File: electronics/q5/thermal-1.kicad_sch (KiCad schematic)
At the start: 6 parts, among them Q3 Charge enable, Q4 Charge enable hot gate

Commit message: Q5 design lock: JLC Basic substitutions, re-verified board, cost estimator
Co-Authored-By: Claude Opus 5.5 <noreply@anthropic.com>
Claude-Session: https://claude.ai/code/session_01UrkzLMrBi6iLPSL5SbMCA7
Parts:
- C9: MPN GRM188R71H104KA93D -> CC0603KRX7R9BB104
- Q3, Q4: MPN 2N7002,215 -> 2N7002
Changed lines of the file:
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@@
       (in_bom yes) (on_board yes) (dnp no)
  (property "Reference" "C9" (at 105.41 73.66 0) (effects (font (size 1.524 1.524)))) (property "Value" "100n" (at 105.41 77.46999999999998 0) (effects (font (size 1.524 1.524))))
-      (property "Footprint" "CountFidgetQ5:Capacitor_SMD_C_0603_1608Metric" (at 105.41 82.55 0) (effects (font (size 1.27 1.27)) (hide yes))) (property "MPN" "GRM188R71H104KA93D" (at 105.41 77.46999999999998 0) (effects (font (size 1.524 1.524)) (hide yes)))
+      (property "Footprint" "CountFidgetQ5:Capacitor_SMD_C_0603_1608Metric" (at 105.41 82.55 0) (effects (font (size 1.27 1.27)) (hide yes))) (property "MPN" "CC0603KRX7R9BB104" (at 105.41 77.46999999999998 0) (effects (font (size 1.524 1.524)) (hide yes)))
       (property "Description" "100 nF local VBUS decoupler beside U5; nearby plane return" (at 105.41 82.55 0) (effects (font (size 1.27 1.27)) (hide yes)))
       (pin "1")(pin "2")
@@
       (in_bom yes) (on_board yes) (dnp no)
  (property "Reference" "Q3" (at 294.64 68.58 0) (effects (font (size 1.524 1.524)))) (property "Value" "Charge enable" (at 294.64 72.38999999999999 0) (effects (font (size 1.524 1.524)) (hide yes)))
-      (property "Footprint" "CountFidgetQ5:Package_TO_SOT_SMD_SOT-23" (at 294.64 82.55 0) (effects (font (size 1.27 1.27)) (hide yes))) (property "MPN" "2N7002,215" (at 294.64 72.38999999999999 0) (effects (font (size 1.524 1.524))))
+      (property "Footprint" "CountFidgetQ5:Package_TO_SOT_SMD_SOT-23" (at 294.64 82.55 0) (effects (font (size 1.27 1.27)) (hide yes))) (property "MPN" "2N7002" (at 294.64 72.38999999999999 0) (effects (font (size 1.524 1.524))))
       (property "Description" "Upper series charge-enable N-MOSFET; gate has ground pulldown" (at 294.64 82.55 0) (effects (font (size 1.27 1.27)) (hide yes)))
       (pin "1")(pin "2")(pin "3")
@@
       (in_bom yes) (on_board yes) (dnp no)
  (property "Reference" "Q4" (at 105.41 147.32 0) (effects (font (size 1.524 1.524)))) (property "Value" "Charge enable hot gate" (at 105.41 151.13 0) (effects (font (size 1.524 1.524)) (hide yes)))
-      (property "Footprint" "CountFidgetQ5:Package_TO_SOT_SMD_SOT-23" (at 105.41 161.29 0) (effects (font (size 1.27 1.27)) (hide yes))) (property "MPN" "2N7002,215" (at 105.41 151.13 0) (effects (font (size 1.524 1.524))))
+      (property "Footprint" "CountFidgetQ5:Package_TO_SOT_SMD_SOT-23" (at 105.41 161.29 0) (effects (font (size 1.27 1.27)) (hide yes))) (property "MPN" "2N7002" (at 105.41 151.13 0) (effects (font (size 1.524 1.524))))
       (property "Description" "Lower series charge-enable N-MOSFET; gate has ground pulldown" (at 105.41 161.29 0) (effects (font (size 1.27 1.27)) (hide yes)))
       (pin "1")(pin "2")(pin "3")

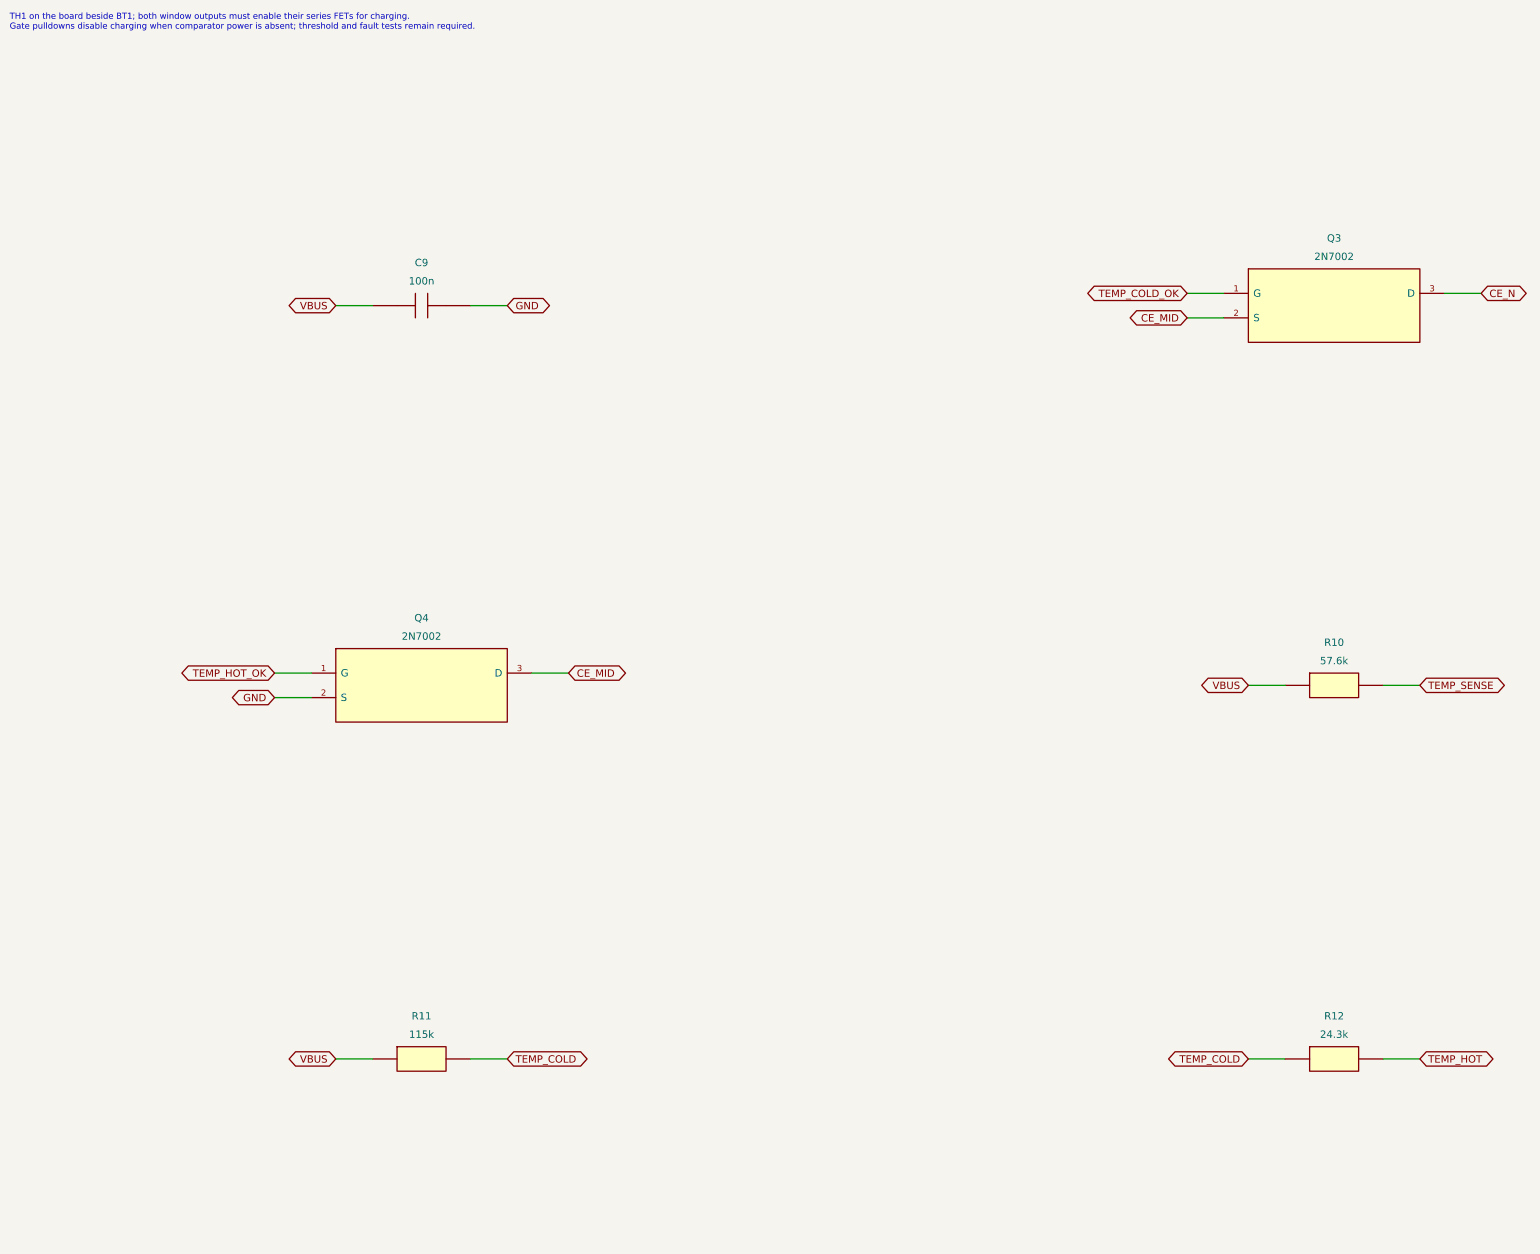
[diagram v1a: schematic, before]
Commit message: First-order de-risking: U5 supply filter, 10 nF latch cap, JLC-corrected CPLs, DFU unplug rule
Three independent checks (datasheet pinouts, JLC EasyEDA footprints, dead-on-arrival
review) found no pinout, footprint or DOA defect. Changes from their findings:
R39 1k + C9 filter U5's 6 V abs-max supply from VBUS hot-plug ringing; C40 10 nF
(min latch press 10.5 ms typ); JLC-corrected CPL files and a preview checklist;
flasher warns to reset a unit left in DFU before unplugging. Board re-routed:
DRC/ERC/parity zero, no via-to-land gaps; emulator 0 failures; stock 43/43.

Co-Authored-By: Claude Opus 5.5 <noreply@anthropic.com>
Claude-Session: https://claude.ai/code/session_01UrkzLMrBi6iLPSL5SbMCA7
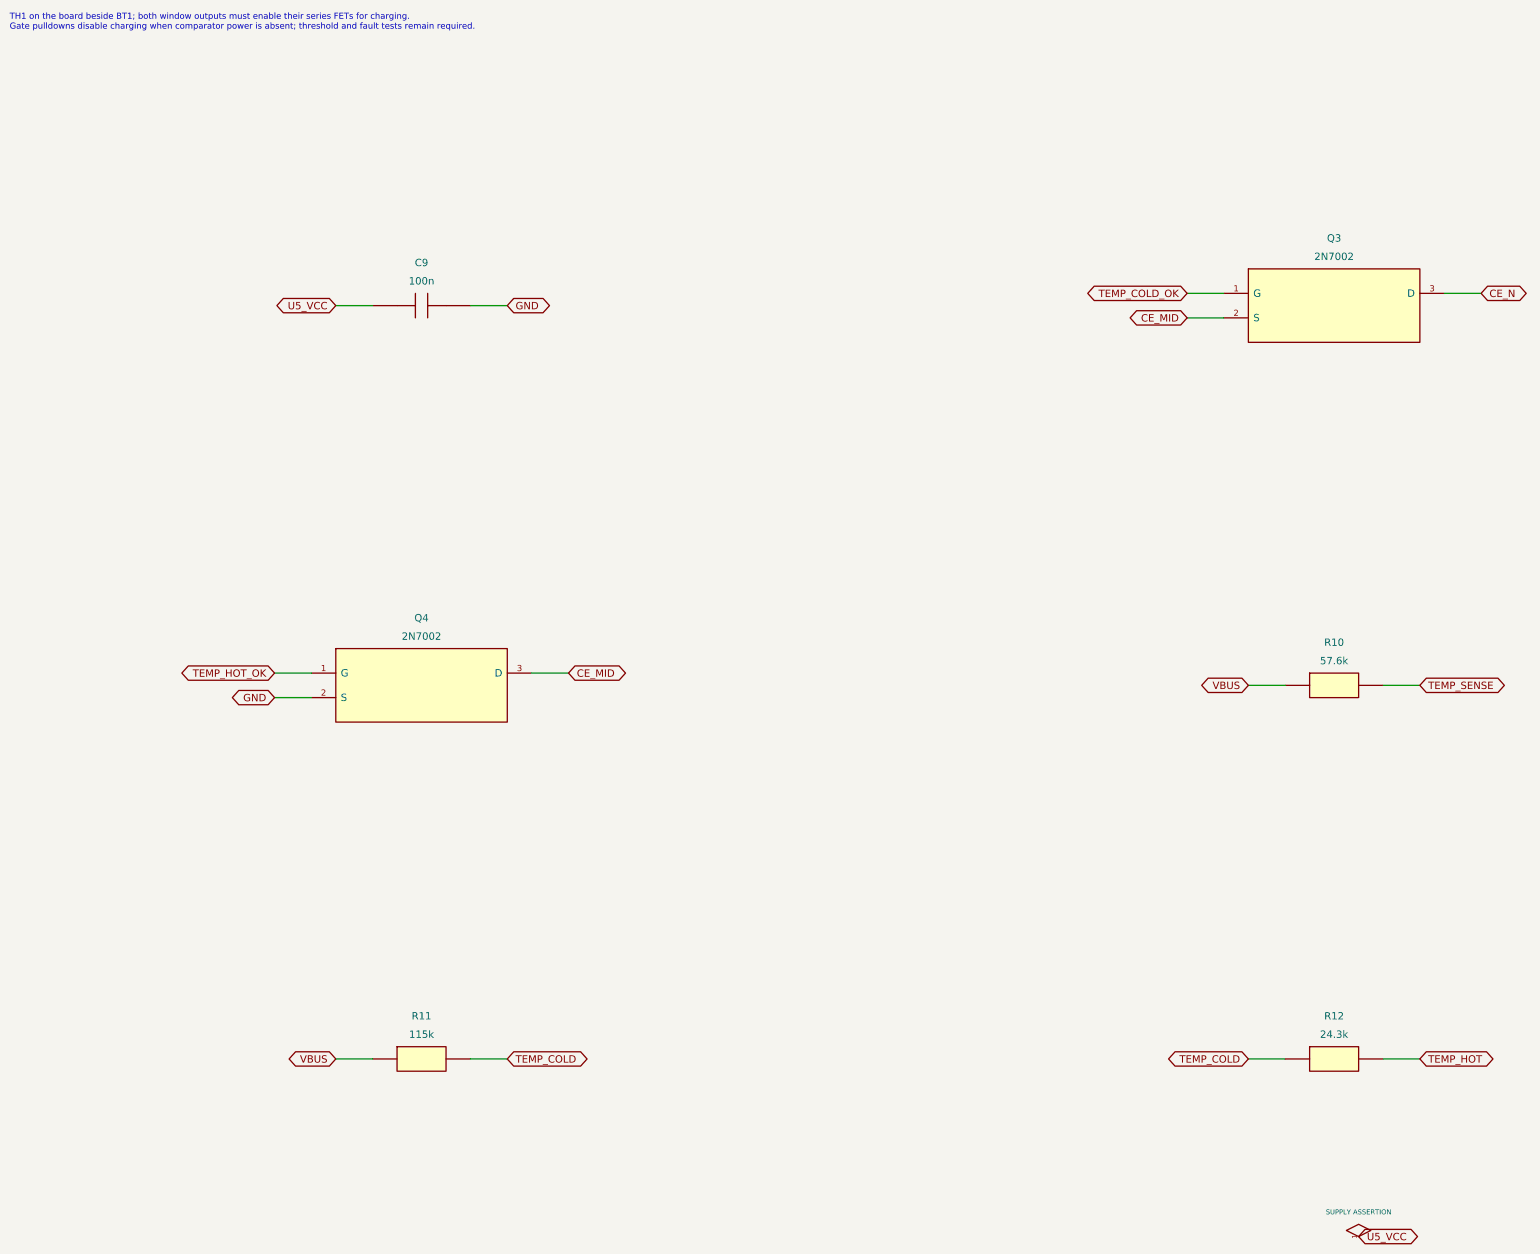
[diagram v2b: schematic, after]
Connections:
- net VBUS: no longer C9.1
- new net U5_VCC: C9.1
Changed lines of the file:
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@@
       (company "Count Fidget") (comment 1 "ENGINEERING CANDIDATE - NOT RELEASED FOR MANUFACTURE"))
 (text "TH1 on the board beside BT1; both window outputs must enable their series FETs for charging.\nGate pulldowns disable charging when comparator power is absent; threshold and fault tests remain required." (at 20 22 0) (effects (font (size 1.27 1.27)) (justify left top)))
+(symbol (lib_id "CountFidgetQ5:SupplyAssertion") (at 299.72 275.59 0) (unit 1)
+      (exclude_from_sim no) (in_bom no) (on_board no) (dnp no)
+      (property "Reference" "#FLG6" (at 299.72 275.59 0) (effects (font (size 1.27 1.27)) (hide yes))) (property "Value" "SUPPLY ASSERTION" (at 299.72 270.51 0) (effects (font (size 1.016 1.016))))
+      (pin "1")
+      (instances (project "click-counter-Q5" (path "/7c190cd8-3ca2-5363-8a92-396d30a08243/aadedfde-0ecd-5e28-8d03-06e68f385e72" (reference "#FLG6") (unit 1)))))
+      (global_label "U5_VCC" (shape bidirectional) (at 299.72 275.59 0)
+      (effects (font (size 1.524 1.524)) (justify left))
+      (property "Intersheetrefs" "${INTERSHEET_REFS}" (at 299.72 275.59 0) (effects (font (size 1.27 1.27)) (hide yes))))
 (symbol (lib_id "CountFidgetQ5:C9") (at 105.41 82.55 0) (unit 1) (exclude_from_sim no)
       (in_bom yes) (on_board yes) (dnp no)
  (property "Reference" "C9" (at 105.41 73.66 0) (effects (font (size 1.524 1.524)))) (property "Value" "100n" (at 105.41 77.46999999999998 0) (effects (font (size 1.524 1.524))))
       (property "Footprint" "CountFidgetQ5:Capacitor_SMD_C_0603_1608Metric" (at 105.41 82.55 0) (effects (font (size 1.27 1.27)) (hide yes))) (property "MPN" "CC0603KRX7R9BB104" (at 105.41 77.46999999999998 0) (effects (font (size 1.524 1.524)) (hide yes)))
-      (property "Description" "100 nF local VBUS decoupler beside U5; nearby plane return" (at 105.41 82.55 0) (effects (font (size 1.27 1.27)) (hide yes)))
+      (property "Description" "100 nF U5 supply decoupler after the R39 1k filter; nearby plane return" (at 105.41 82.55 0) (effects (font (size 1.27 1.27)) (hide yes)))
       (pin "1")(pin "2")
       (instances (project "click-counter-Q5" (path "/7c190cd8-3ca2-5363-8a92-396d30a08243/aadedfde-0ecd-5e28-8d03-06e68f385e72" (reference "C9") (unit 1)))))
 (wire (pts (xy 95.25 82.55) (xy 87.63 82.55)) (stroke (width 0) (type default)))
-(global_label "VBUS" (shape bidirectional) (at 87.63 82.55 180)
+(global_label "U5_VCC" (shape bidirectional) (at 87.63 82.55 180)
       (effects (font (size 1.524 1.524)) (justify right))
       (property "Intersheetrefs" "${INTERSHEET_REFS}" (at 87.63 82.55 0) (effects (font (size 1.27 1.27)) (hide yes))))
